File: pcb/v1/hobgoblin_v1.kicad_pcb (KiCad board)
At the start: 2 copper layers, 160 x 115 mm, 55 parts, among them J1 5V, J2 RC2014EXT1, J3 RC2014EXT2, J4 USB_B_Mini, SW1 RESET, SW2 ROMBNK, U1 74LS32, U10 FT232RL, U2 Z80CPU, U3 74LS14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

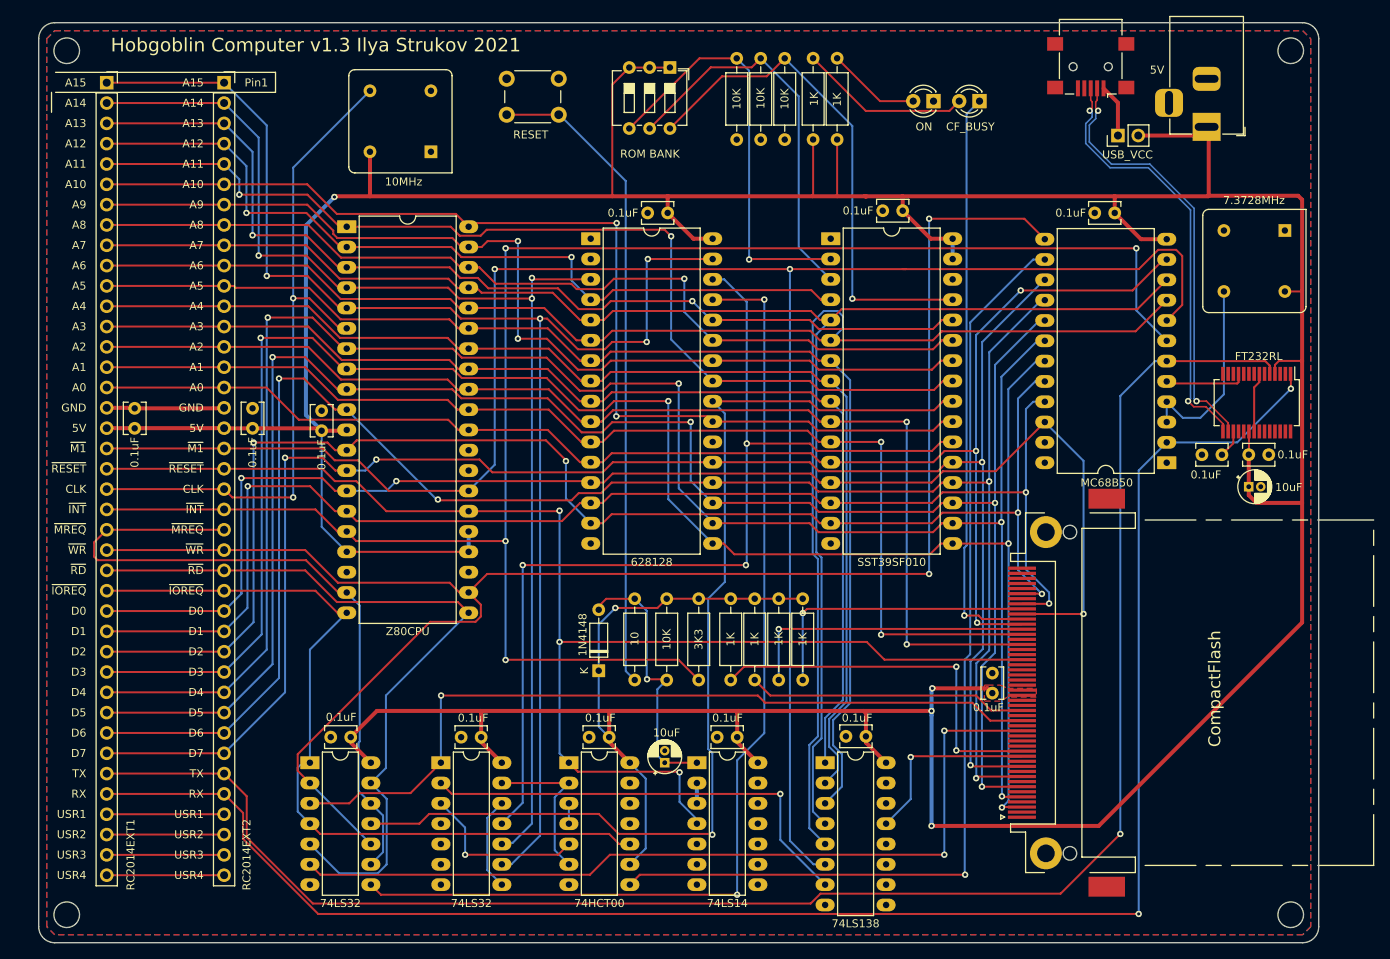
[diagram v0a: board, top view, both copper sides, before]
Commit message: Convert PCB files to KiCAD v6
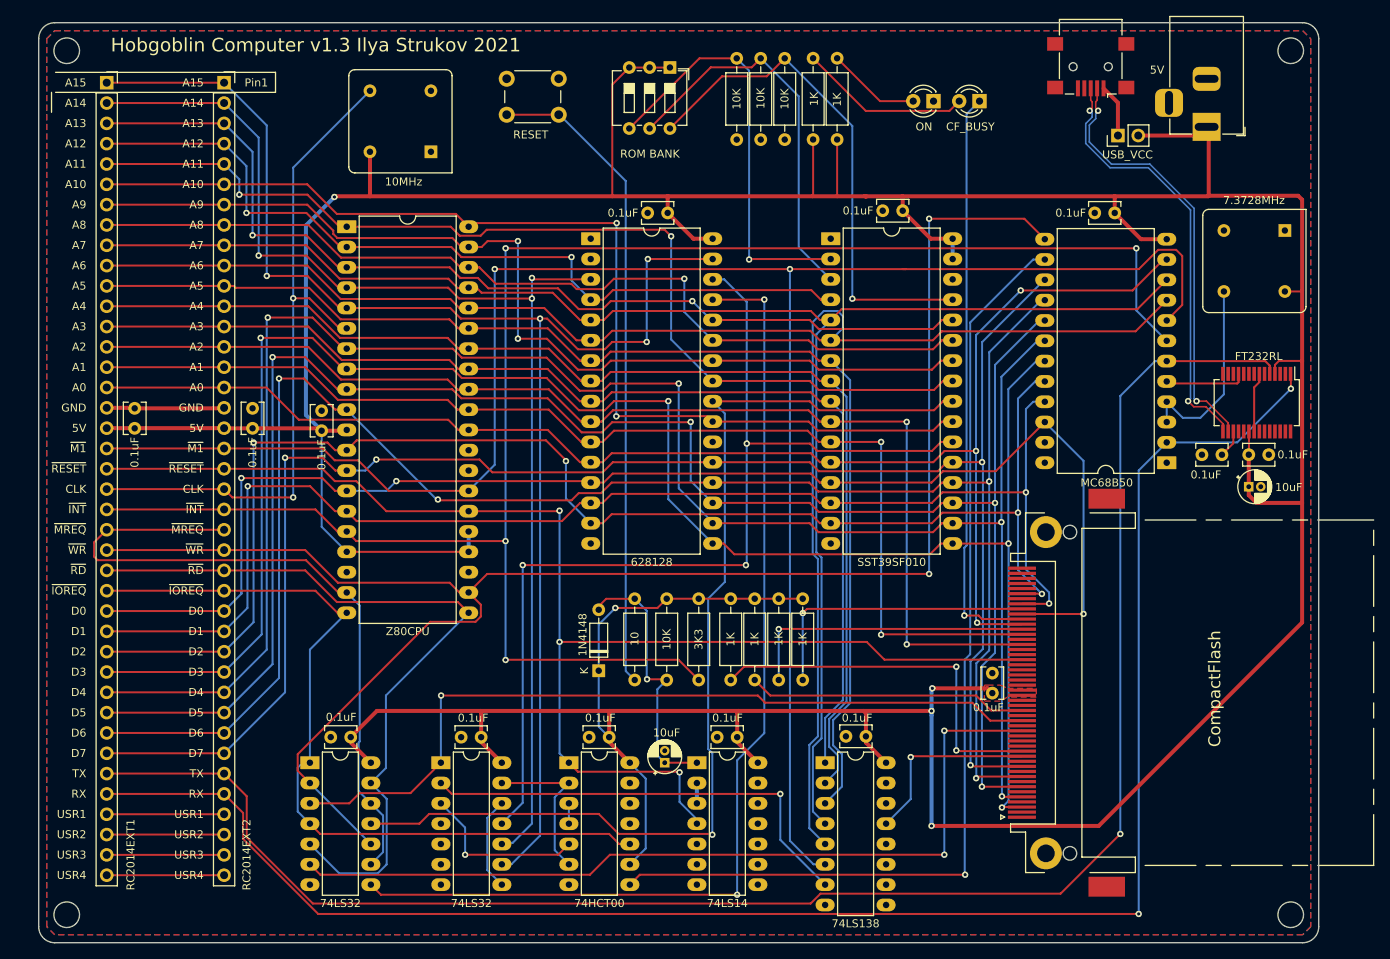
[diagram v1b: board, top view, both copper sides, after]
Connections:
- net /RAM\~ROM renamed /RAM\~{ROM}
- net /~INT renamed /~{INT}
- net /~IORD renamed /~{IORD}
- net /~IORQ renamed /~{IORQ}
- net /~IOWR renamed /~{IOWR}
- net /~LOW16K renamed /~{LOW16K}
- net /~M1 renamed /~{M1}
- net /~MEMRD renamed /~{MEMRD}
- net /~MEMWR renamed /~{MEMWR}
- net /~MREQ renamed /~{MREQ}
- net /~PORT10 renamed /~{PORT10}
- net /~PORT38 renamed /~{PORT38}
- net /~RD renamed /~{RD}
- net /~RESET renamed /~{RESET}
- net /~ROMOFF renamed /~{ROMOFF}
- net /~ROM_DISABLED renamed /~{ROM_DISABLED}
- net /~RTS renamed /~{RTS}
- net /~WR renamed /~{WR}
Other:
- net class Default removed

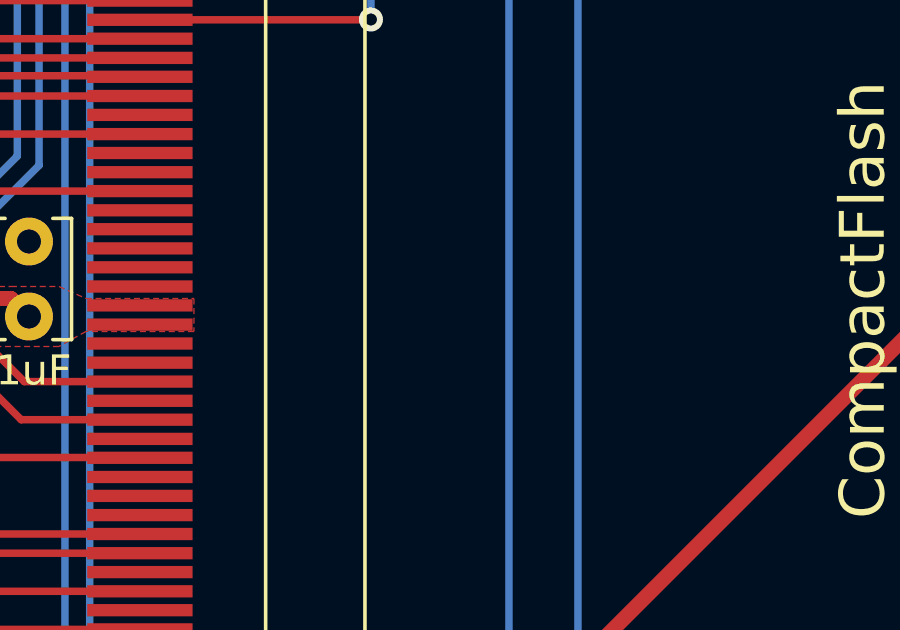
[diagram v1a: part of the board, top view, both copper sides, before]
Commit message: Rename CF Card connector footprint to match the actual part
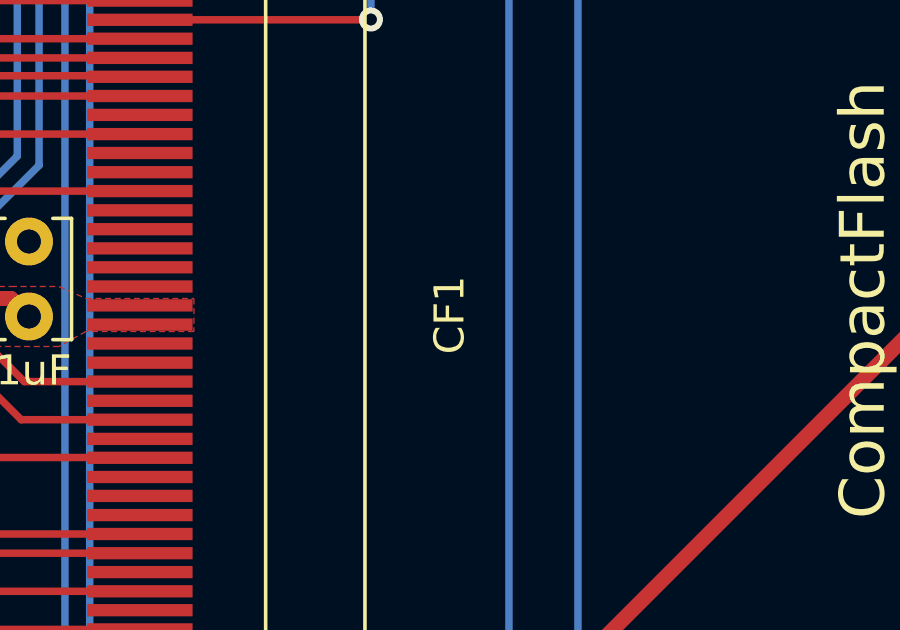
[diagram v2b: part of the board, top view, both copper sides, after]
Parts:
- CF1: footprint hobgoblin:CF-Card_3M_N7E50-7516PK-20-WF -> hobgoblin:CF-Card_3M_N7E507516PK20
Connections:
- CF1 pad 24: Net-(CF1-Pad24) -> unconnected-(CF1-Pad24)
- CF1 pad 25: Net-(CF1-Pad25) -> unconnected-(CF1-Pad25)
- CF1 pad 26: Net-(CF1-Pad26) -> unconnected-(CF1-Pad26)
- CF1 pad 27: Net-(CF1-Pad27) -> unconnected-(CF1-Pad27)
- CF1 pad 28: Net-(CF1-Pad28) -> unconnected-(CF1-Pad28)
- CF1 pad 29: Net-(CF1-Pad29) -> unconnected-(CF1-Pad29)
- CF1 pad 30: Net-(CF1-Pad30) -> unconnected-(CF1-Pad30)
- CF1 pad 31: Net-(CF1-Pad31) -> unconnected-(CF1-Pad31)
- CF1 pad 33: Net-(CF1-Pad33) -> unconnected-(CF1-Pad33)
- CF1 pad 37: Net-(CF1-Pad37) -> unconnected-(CF1-Pad37)
- CF1 pad 40: Net-(CF1-Pad40) -> unconnected-(CF1-Pad40)
- CF1 pad 42: Net-(CF1-Pad42) -> unconnected-(CF1-Pad42)
- CF1 pad 43: Net-(CF1-Pad43) -> unconnected-(CF1-Pad43)
- CF1 pad 47: Net-(CF1-Pad47) -> unconnected-(CF1-Pad47)
- CF1 pad 48: Net-(CF1-Pad48) -> unconnected-(CF1-Pad48)
- CF1 pad 49: Net-(CF1-Pad49) -> unconnected-(CF1-Pad49)
- J4 pad 4: Net-(J4-Pad4) -> unconnected-(J4-Pad4)
- U10 pad 10: Net-(U10-Pad10) -> unconnected-(U10-Pad10)
- U10 pad 12: Net-(U10-Pad12) -> unconnected-(U10-Pad12)
- U10 pad 13: Net-(U10-Pad13) -> unconnected-(U10-Pad13)
- U10 pad 14: Net-(U10-Pad14) -> unconnected-(U10-Pad14)
- U10 pad 19: Net-(U10-Pad19) -> unconnected-(U10-Pad19)
- U10 pad 2: Net-(U10-Pad2) -> unconnected-(U10-Pad2)
- U10 pad 22: Net-(U10-Pad22) -> unconnected-(U10-Pad22)
- U10 pad 23: Net-(U10-Pad23) -> unconnected-(U10-Pad23)
- U10 pad 27: Net-(U10-Pad27) -> unconnected-(U10-Pad27)
- U10 pad 28: Net-(U10-Pad28) -> unconnected-(U10-Pad28)
- U10 pad 3: Net-(U10-Pad3) -> unconnected-(U10-Pad3)
- U10 pad 6: Net-(U10-Pad6) -> unconnected-(U10-Pad6)
- U10 pad 9: Net-(U10-Pad9) -> unconnected-(U10-Pad9)
- U2 pad 18: Net-(U2-Pad18) -> unconnected-(U2-Pad18)
- U2 pad 23: Net-(U2-Pad23) -> unconnected-(U2-Pad23)
- U2 pad 28: Net-(U2-Pad28) -> unconnected-(U2-Pad28)
- U4 pad 10: Net-(U4-Pad10) -> unconnected-(U4-Pad10)
- U4 pad 11: Net-(U4-Pad11) -> unconnected-(U4-Pad11)
- U4 pad 12: Net-(U4-Pad12) -> unconnected-(U4-Pad12)
- U4 pad 14: Net-(U4-Pad14) -> unconnected-(U4-Pad14)
- U4 pad 15: Net-(U4-Pad15) -> unconnected-(U4-Pad15)
- U4 pad 9: Net-(U4-Pad9) -> unconnected-(U4-Pad9)
- U5 pad 1: Net-(U5-Pad1) -> unconnected-(U5-Pad1)
- X1 pad 1: Net-(X1-Pad1) -> unconnected-(X1-Pad1)
- X2 pad 1: Net-(X2-Pad1) -> unconnected-(X2-Pad1)
